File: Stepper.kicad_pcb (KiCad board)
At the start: 2 copper layers, 85 x 65 mm, 67 parts, among them J1 Conn_02x18_Counter_Clockwise, SW1 STEP, SW2 RESET, SW3 MANUAL/~{AUTO}, X1 Power, X2 Address, X3 Data, X4 Mode, X5 Control, X6 Clock

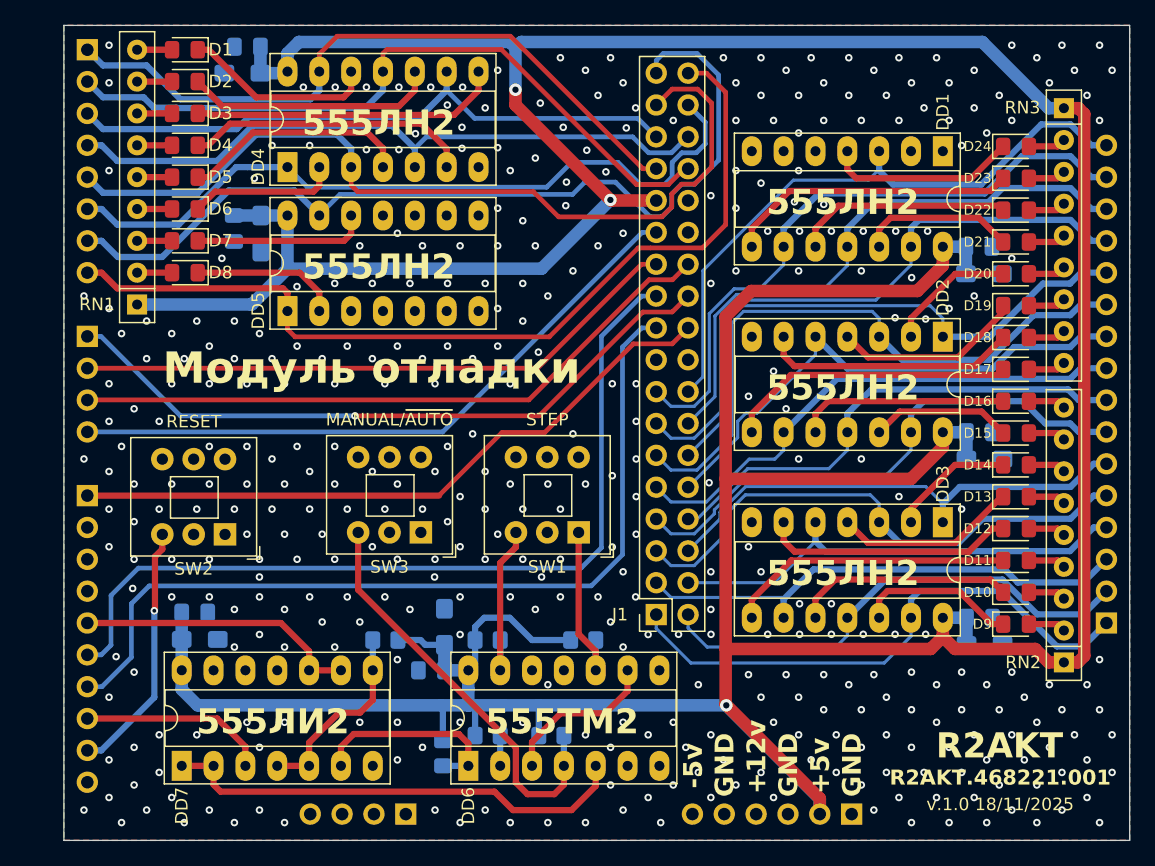
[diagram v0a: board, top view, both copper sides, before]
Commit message: Add files via upload
Fix button error and missed ground.
Исправлена ошибка кнопок и отсутствующих земель.
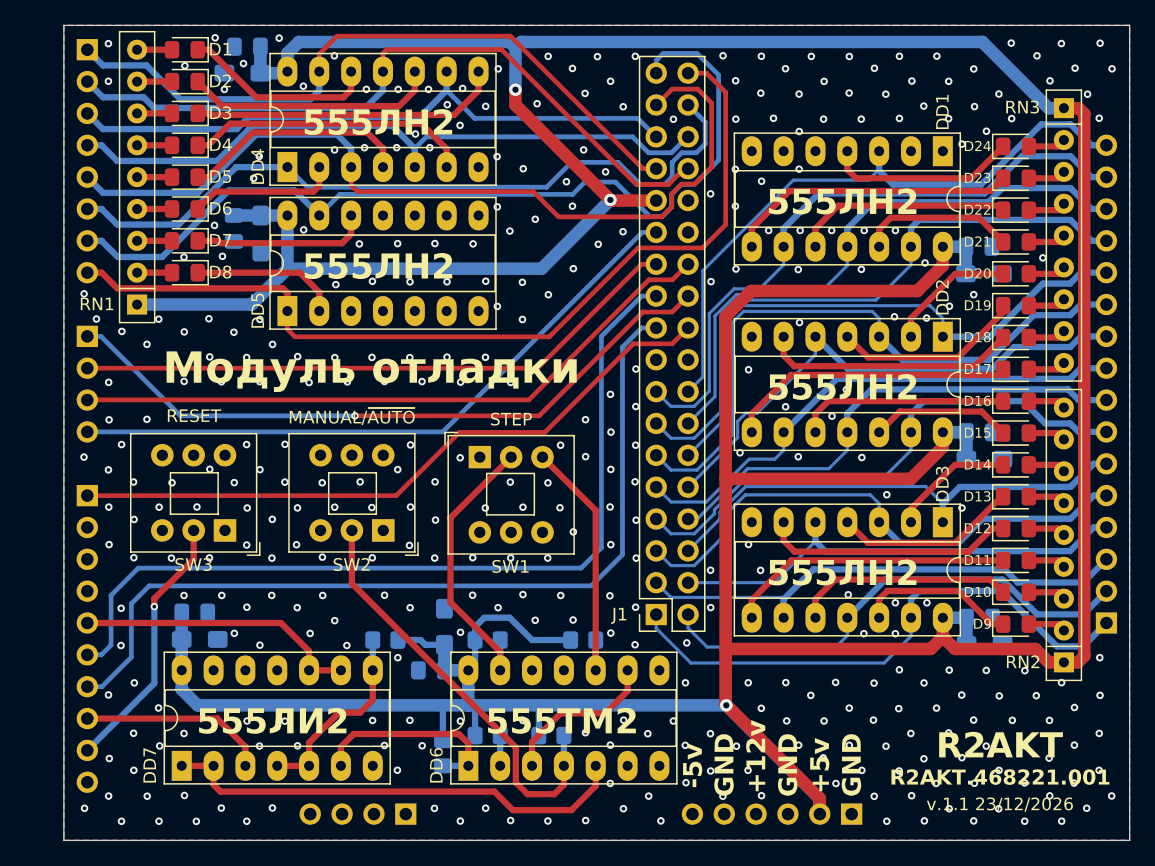
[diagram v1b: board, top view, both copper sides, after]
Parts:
- SW2: value RESET -> MANUAL/~{AUTO}
- SW3: value MANUAL/~{AUTO} -> RESET
- moved SW3 15.6 mm to (85.2, 109.9)
- moved SW2 12.6 mm to (97.8, 109.9)
- moved SW1 9.91 mm to (105.5, 104.0), turned to 0 degrees
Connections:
- DD6 pad 11: unconnected-(DD6B-C-Pad11) -> GND
- DD6 pad 12: unconnected-(DD6B-D-Pad12) -> GND
- SW1 pad 1: Net-(DD6B-~{S}) -> GND
- SW1 pad 2: GND -> Net-(DD6B-~{R})
- SW1 pad 3: Net-(DD6B-~{R}) -> Net-(DD6B-~{S})
- SW2 pad 1: unconnected-(SW2-A-Pad1) -> GND
- SW2 pad 2: GND -> Net-(DD6A-~{S})
- SW2 pad 3: /~{RESIN} -> unconnected-(SW2-A-Pad3)
- SW3 pad 1: unconnected-(SW3-A-Pad1) -> GND
- SW3 pad 2: GND -> /~{RESIN}
- SW3 pad 3: Net-(DD6A-~{S}) -> unconnected-(SW3-A-Pad3)
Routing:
- net Net-(DD6B-~{R}): track 13.9 -> 23.1 mm
- net Net-(DD6B-~{S}): track 14.0 -> 21.2 mm
- net /~{RESIN}: track 20.4 -> 20.9 mm
- net GND: track 0.00 -> 0.22 mm, vias 392 -> 375
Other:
- board text added: "v.1.1 23/12/2026"
- board text removed: "v.1.0 18/11/2025"

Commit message: Add files via upload
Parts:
- moved REF** 1.70 mm to (113.3, 87.2), turned to 90 degrees
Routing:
- net Net-(DD6A-~{S}): track 34.0 -> 36.4 mm
- net Net-(DD6A-D): track 2.41 -> 0.00 mm
- net GND: vias 375 -> 455
